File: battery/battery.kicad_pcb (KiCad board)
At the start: 2 copper layers, 73.7 x 63.5 mm, 40 parts, among them J1 batt_1, J2 batt_2, J3 batt_3, J4 batt_4, J5 reed_switch, J6 toPcb+, J7 toPcb-, J8 on_signal, Q1 batt1_sw, Q2 batt2_sw, Q3 batt3_sw, Q4 batt4_sw, Q5 Q_NPN_CBE, U1 LM1117-5.0, U2 LTV-817S

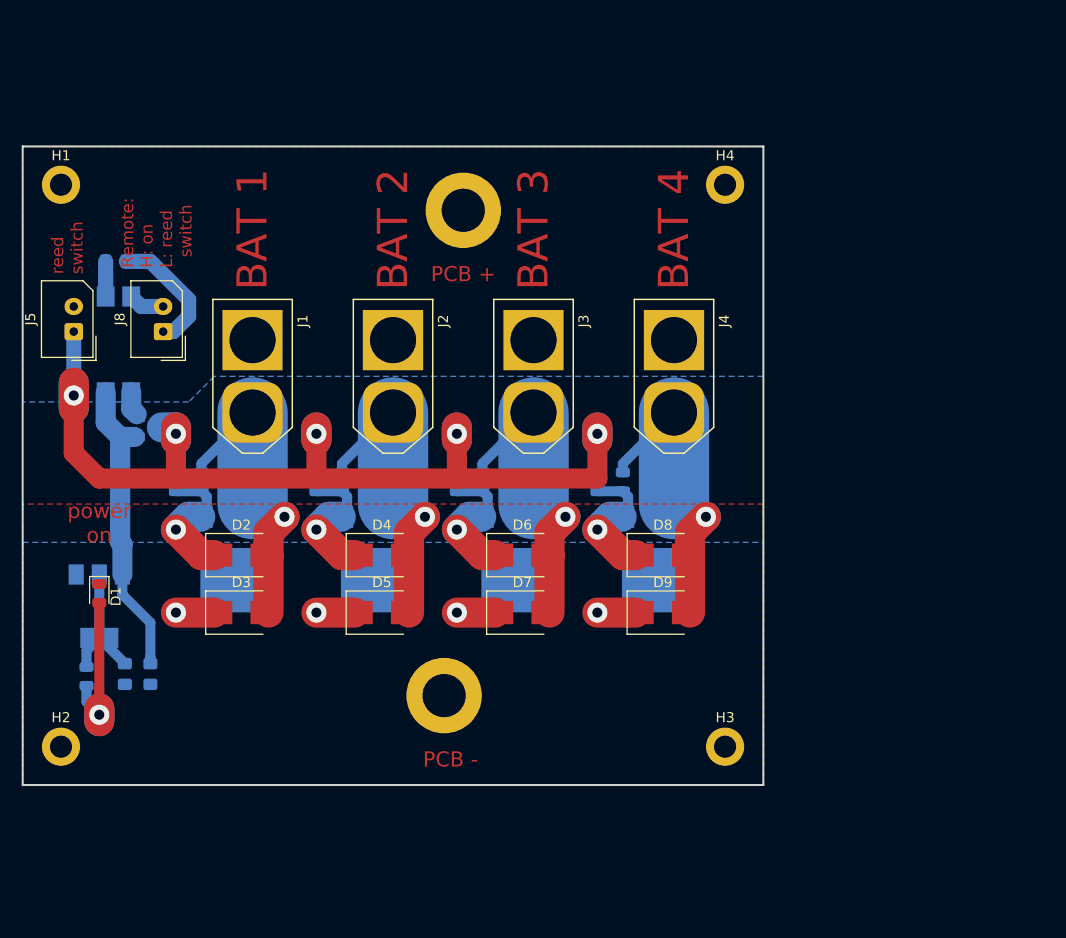
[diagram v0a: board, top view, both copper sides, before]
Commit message: capacitor bybpas
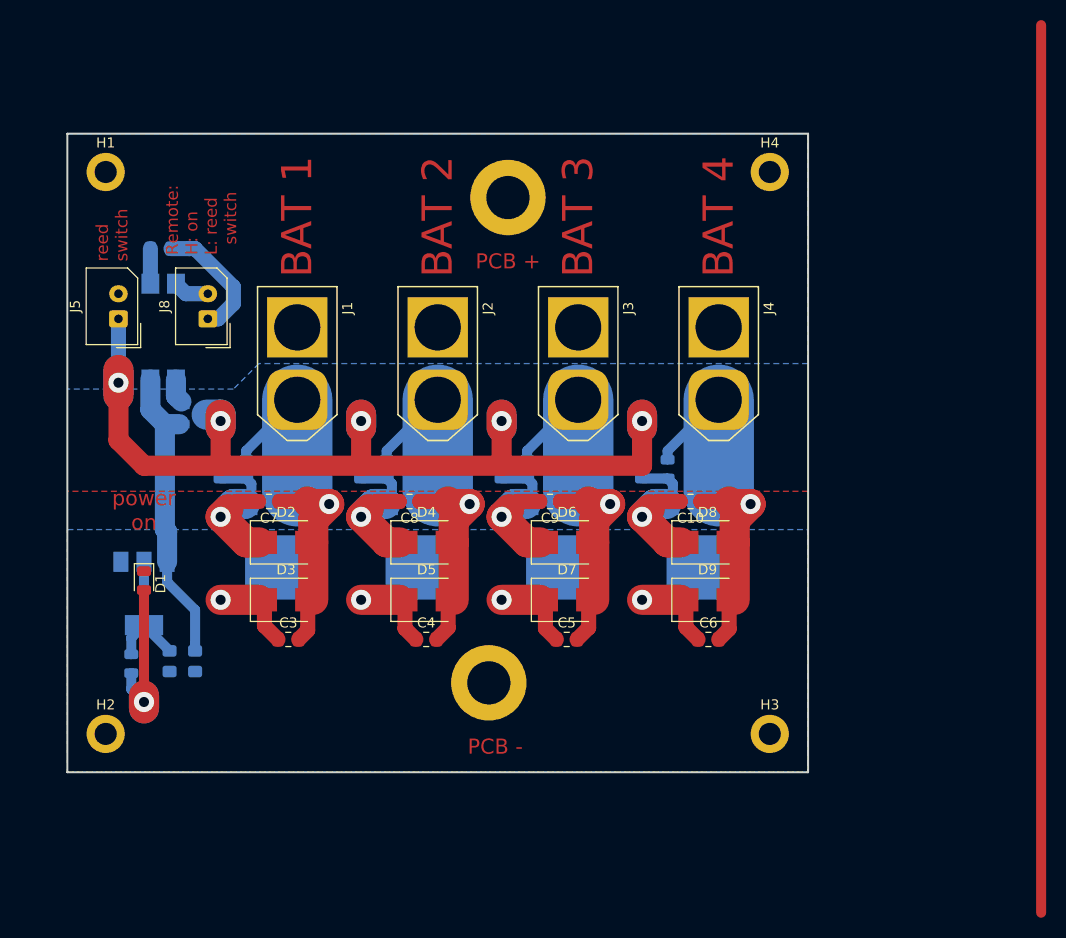
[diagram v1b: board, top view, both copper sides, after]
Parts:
- added C10: 100n, Capacitor_SMD:C_0805_2012Metric_Pad1.15x1.40mm_HandSolder, F.Cu at (117.2, 100.1)
- added C3: 10uF, Capacitor_SMD:C_0805_2012Metric_Pad1.15x1.40mm_HandSolder, F.Cu at (77.2, 113.8)
- added C4: 10uF, Capacitor_SMD:C_0805_2012Metric_Pad1.15x1.40mm_HandSolder, F.Cu at (90.9, 113.8)
- added C5: 10uF, Capacitor_SMD:C_0805_2012Metric_Pad1.15x1.40mm_HandSolder, F.Cu at (104.9, 113.8)
- added C6: 10uF, Capacitor_SMD:C_0805_2012Metric_Pad1.15x1.40mm_HandSolder, F.Cu at (119.0, 113.8)
- added C7: 100n, Capacitor_SMD:C_0805_2012Metric_Pad1.15x1.40mm_HandSolder, F.Cu at (75.3, 100.1)
- added C8: 100n, Capacitor_SMD:C_0805_2012Metric_Pad1.15x1.40mm_HandSolder, F.Cu at (89.3, 100.1)
- added C9: 100n, Capacitor_SMD:C_0805_2012Metric_Pad1.15x1.40mm_HandSolder, F.Cu at (103.2, 100.1)
- C1, C2: value 100n -> C_Small
- moved J6 4.62 mm to (99.1, 69.8)
- moved D2 4.62 mm to (77.0, 104.1)
- moved D3 4.62 mm to (77.0, 109.9)
- moved D4 4.62 mm to (91.0, 104.1)
- moved D5 4.62 mm to (91.0, 109.9)
- moved D6 4.62 mm to (104.9, 104.1)
- moved D7 4.62 mm to (104.9, 109.9)
- moved D8 4.62 mm to (118.9, 104.1)
- moved D9 4.62 mm to (118.9, 109.9)
- moved J1 4.62 mm to (78.1, 86.4)
- moved J2 4.62 mm to (92.1, 86.4)
- moved J3 4.62 mm to (106.0, 86.4)
- moved J4 4.62 mm to (120.0, 86.4)
- moved J7 4.62 mm to (97.2, 118.1)
- moved J8 4.62 mm to (69.2, 81.9)
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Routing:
- net (no net): track 0.00 -> 88.3 mm
- net gnd: track 15.2 -> 33.0 mm
- net Net-(C4-Pad2): track 29.2 -> 43.8 mm
- net Net-(C5-Pad2): track 29.2 -> 43.8 mm
- net Net-(C10-Pad1): track 29.2 -> 43.7 mm
- net Net-(C3-Pad2): track 31.0 -> 40.4 mm
- net Net-(C8-Pad2): track 13.6 -> 21.4 mm
- net Net-(C9-Pad2): track 13.1 -> 20.9 mm
- net Net-(C10-Pad2): track 13.1 -> 20.9 mm
- net Net-(C7-Pad2): track 13.1 -> 18.6 mm

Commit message: fix
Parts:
- removed the C1 at (65.4, 116.0)
- removed the C10 at (117.2, 100.1)
- removed the C2 at (67.9, 116.0)
- removed the C3 at (77.2, 113.8)
- removed the C4 at (90.9, 113.8)
- removed the C5 at (104.9, 113.8)
- removed the C6 at (119.0, 113.8)
- removed the C7 at (75.3, 100.1)
- removed the C8 at (89.3, 100.1)
- removed the C9 at (103.2, 100.1)
- removed the D1 at (62.9, 108.0)
- removed the D2 at (77.0, 104.1)
- removed the D3 at (77.0, 109.9)
- removed the D4 at (91.0, 104.1)
- removed the D5 at (91.0, 109.9)
- removed the D6 at (104.9, 104.1)
- removed the D7 at (104.9, 109.9)
- removed the D8 at (118.9, 104.1)
- removed the D9 at (118.9, 109.9)
- removed the H1 at (59.1, 67.3)
- removed the H2 at (59.1, 123.2)
- removed the H3 at (125.1, 123.2)
- removed the H4 at (125.1, 67.3)
- removed the J1 at (78.1, 86.4)
- removed the J2 at (92.1, 86.4)
- removed the J3 at (106.0, 86.4)
- removed the J4 at (120.0, 86.4)
- removed the J5 at (60.3, 81.9)
- removed the J6 at (99.1, 69.8)
- removed the J7 at (97.2, 118.1)
- removed the J8 at (69.2, 81.9)
- removed the Q1 at (75.8, 104.5)
- removed the Q2 at (89.8, 104.5)
- removed the Q3 at (103.8, 104.5)
- removed the Q4 at (117.7, 104.5)
- removed the Q5 at (67.9, 91.4)
- removed the R1 at (61.6, 116.2)
- removed the R10 at (64.5, 74.9)
- removed the R2 at (70.5, 96.9)
- removed the R3 at (84.5, 96.9)
- removed the R4 at (98.4, 96.9)
- removed the R5 at (112.4, 96.9)
- removed the R6 at (73.0, 96.9)
- removed the R7 at (87.0, 96.9)
- removed the R8 at (101.0, 96.9)
- removed the R9 at (114.9, 96.9)
- removed the U1 at (62.9, 109.2)
- removed the U2 at (64.8, 83.2)
- added C1: C_Small, Capacitor_SMD:C_0805_2012Metric_Pad1.15x1.40mm_HandSolder, B.Cu at (204.7, 68.6)
- added C1: C_Small, Capacitor_SMD:C_0805_2012Metric_Pad1.15x1.40mm_HandSolder, F.Cu at (131.8, 68.6)
- added C10: 100n, Capacitor_SMD:C_0805_2012Metric_Pad1.15x1.40mm_HandSolder, F.Cu at (220.6, 120.4)
- added C10: 100n, Capacitor_SMD:C_0805_2012Metric_Pad1.15x1.40mm_HandSolder, B.Cu at (116.0, 120.4)
- added C2: C_Small, Capacitor_SMD:C_0805_2012Metric_Pad1.15x1.40mm_HandSolder, B.Cu at (204.7, 71.1)
- added C2: C_Small, Capacitor_SMD:C_0805_2012Metric_Pad1.15x1.40mm_HandSolder, F.Cu at (131.8, 71.1)
- added C3: 10uF, Capacitor_SMD:C_0805_2012Metric_Pad1.15x1.40mm_HandSolder, F.Cu at (206.9, 80.4)
- added C3: 10uF, Capacitor_SMD:C_0805_2012Metric_Pad1.15x1.40mm_HandSolder, B.Cu at (129.7, 80.4)
- added C4: 10uF, Capacitor_SMD:C_0805_2012Metric_Pad1.15x1.40mm_HandSolder, F.Cu at (206.9, 94.1)
- added C4: 10uF, Capacitor_SMD:C_0805_2012Metric_Pad1.15x1.40mm_HandSolder, B.Cu at (129.7, 94.1)
- added C5: 10uF, Capacitor_SMD:C_0805_2012Metric_Pad1.15x1.40mm_HandSolder, F.Cu at (206.9, 108.1)
- added C5: 10uF, Capacitor_SMD:C_0805_2012Metric_Pad1.15x1.40mm_HandSolder, B.Cu at (129.7, 108.1)
- added C6: 10uF, Capacitor_SMD:C_0805_2012Metric_Pad1.15x1.40mm_HandSolder, F.Cu at (206.9, 122.2)
- added C6: 10uF, Capacitor_SMD:C_0805_2012Metric_Pad1.15x1.40mm_HandSolder, B.Cu at (129.7, 122.2)
- added C7: 100n, Capacitor_SMD:C_0805_2012Metric_Pad1.15x1.40mm_HandSolder, F.Cu at (220.6, 78.5)
- added C7: 100n, Capacitor_SMD:C_0805_2012Metric_Pad1.15x1.40mm_HandSolder, B.Cu at (116.0, 78.5)
- added C8: 100n, Capacitor_SMD:C_0805_2012Metric_Pad1.15x1.40mm_HandSolder, F.Cu at (220.6, 92.4)
- added C8: 100n, Capacitor_SMD:C_0805_2012Metric_Pad1.15x1.40mm_HandSolder, B.Cu at (116.0, 92.4)
- added C9: 100n, Capacitor_SMD:C_0805_2012Metric_Pad1.15x1.40mm_HandSolder, F.Cu at (220.6, 106.4)
- added C9: 100n, Capacitor_SMD:C_0805_2012Metric_Pad1.15x1.40mm_HandSolder, B.Cu at (116.0, 106.4)
- added D1: power_ok, LED_SMD:LED_0805_2012Metric, F.Cu at (212.7, 66.0)
- added D1: power_ok, LED_SMD:LED_0805_2012Metric, B.Cu at (123.8, 66.0)
- added D2: D_TVS, Diode_SMD:D_SMB, F.Cu at (216.5, 80.2)
- added D2: D_TVS, Diode_SMD:D_SMB, B.Cu at (120.0, 80.2)
- added D3: D_TVS, Diode_SMD:D_SMB, F.Cu at (210.8, 80.2)
- added D3: D_TVS, Diode_SMD:D_SMB, B.Cu at (125.7, 80.2)
- added D4: D_TVS, Diode_SMD:D_SMB, F.Cu at (216.5, 94.1)
- added D4: D_TVS, Diode_SMD:D_SMB, B.Cu at (120.0, 94.1)
- added D5: D_TVS, Diode_SMD:D_SMB, F.Cu at (210.8, 94.1)
- added D5: D_TVS, Diode_SMD:D_SMB, B.Cu at (125.7, 94.1)
- added D6: D_TVS, Diode_SMD:D_SMB, F.Cu at (216.5, 108.1)
- added D6: D_TVS, Diode_SMD:D_SMB, B.Cu at (120.0, 108.1)
- added D7: D_TVS, Diode_SMD:D_SMB, F.Cu at (210.8, 108.1)
- added D7: D_TVS, Diode_SMD:D_SMB, B.Cu at (125.7, 108.1)
- added D8: D_TVS, Diode_SMD:D_SMB, F.Cu at (216.5, 122.1)
- added D8: D_TVS, Diode_SMD:D_SMB, B.Cu at (120.0, 122.1)
- added D9: D_TVS, Diode_SMD:D_SMB, F.Cu at (210.8, 122.1)
- added D9: D_TVS, Diode_SMD:D_SMB, B.Cu at (125.7, 122.1)
- added H1: mnt, MountingHole:MountingHole_2.2mm_M2_DIN965_Pad, F.Cu at (253.4, 62.2)
- added H1: mnt, MountingHole:MountingHole_2.2mm_M2_DIN965_Pad, B.Cu at (83.2, 62.2)
- added H2: mnt, MountingHole:MountingHole_2.2mm_M2_DIN965_Pad, F.Cu at (197.5, 62.2)
- added H2: mnt, MountingHole:MountingHole_2.2mm_M2_DIN965_Pad, B.Cu at (139.1, 62.2)
- added H3: mnt, MountingHole:MountingHole_2.2mm_M2_DIN965_Pad, F.Cu at (197.5, 128.3)
- added H3: mnt, MountingHole:MountingHole_2.2mm_M2_DIN965_Pad, B.Cu at (139.1, 128.3)
- added H4: mnt, MountingHole:MountingHole_2.2mm_M2_DIN965_Pad, F.Cu at (253.4, 128.3)
- added H4: mnt, MountingHole:MountingHole_2.2mm_M2_DIN965_Pad, B.Cu at (83.2, 128.3)
- added J1: batt_1, power_connectors:XT60UPB-M, F.Cu at (234.3, 81.3)
- added J1: batt_1, power_connectors:XT60UPB-M, B.Cu at (102.2, 81.3)
- added J2: batt_2, power_connectors:XT60UPB-M, F.Cu at (234.3, 95.2)
- added J2: batt_2, power_connectors:XT60UPB-M, B.Cu at (102.2, 95.2)
- added J3: batt_3, power_connectors:XT60UPB-M, F.Cu at (234.3, 109.2)
- added J3: batt_3, power_connectors:XT60UPB-M, B.Cu at (102.2, 109.2)
- added J4: batt_4, power_connectors:XT60UPB-M, F.Cu at (234.3, 123.2)
- added J4: batt_4, power_connectors:XT60UPB-M, B.Cu at (102.2, 123.2)
- added J5: reed_switch, Connector_Molex:Molex_SPOX_5267-02A_1x02_P2.50mm_Vertical, F.Cu at (238.8, 63.5)
- added J5: reed_switch, Connector_Molex:Molex_SPOX_5267-02A_1x02_P2.50mm_Vertical, B.Cu at (97.8, 63.5)
- added J6: toPcb+, MountingHole:MountingHole_4.3mm_M4_DIN965_Pad, B.Cu at (250.8, 102.2)
- added J6: toPcb+, MountingHole:MountingHole_4.3mm_M4_DIN965_Pad, F.Cu at (85.7, 102.2)
- added J7: toPcb-, MountingHole:MountingHole_4.3mm_M4_DIN965_Pad, B.Cu at (202.6, 100.3)
- added J7: toPcb-, MountingHole:MountingHole_4.3mm_M4_DIN965_Pad, F.Cu at (134.0, 100.3)
- added J8: on_signal, Connector_Molex:Molex_SPOX_5267-02A_1x02_P2.50mm_Vertical, F.Cu at (238.8, 72.4)
- added J8: on_signal, Connector_Molex:Molex_SPOX_5267-02A_1x02_P2.50mm_Vertical, B.Cu at (97.8, 72.4)
- added Q1: batt1_sw, Package_TO_SOT_SMD:TO-252-2, B.Cu at (216.1, 79.0)
- added Q1: batt1_sw, Package_TO_SOT_SMD:TO-252-2, F.Cu at (120.4, 79.0)
- added Q2: batt2_sw, Package_TO_SOT_SMD:TO-252-2, B.Cu at (216.1, 93.0)
- added Q2: batt2_sw, Package_TO_SOT_SMD:TO-252-2, F.Cu at (120.4, 93.0)
- added Q3: batt3_sw, Package_TO_SOT_SMD:TO-252-2, B.Cu at (216.1, 106.9)
- added Q3: batt3_sw, Package_TO_SOT_SMD:TO-252-2, F.Cu at (120.4, 106.9)
- added Q4: batt4_sw, Package_TO_SOT_SMD:TO-252-2, B.Cu at (216.1, 120.9)
- added Q4: batt4_sw, Package_TO_SOT_SMD:TO-252-2, F.Cu at (120.4, 120.9)
- added Q5: Q_NPN_CBE, Package_TO_SOT_SMD:SOT-23, B.Cu at (229.2, 71.1)
- added Q5: Q_NPN_CBE, Package_TO_SOT_SMD:SOT-23, F.Cu at (107.3, 71.1)
- added R1: 400, Resistor_SMD:R_0805_2012Metric, B.Cu at (204.5, 64.8)
- added R1: 400, Resistor_SMD:R_0805_2012Metric, F.Cu at (132.1, 64.8)
- added R10: R, Resistor_SMD:R_0805_2012Metric_Pad1.15x1.40mm_HandSolder, B.Cu at (245.7, 67.7)
- added R10: R, Resistor_SMD:R_0805_2012Metric_Pad1.15x1.40mm_HandSolder, F.Cu at (90.8, 67.7)
- added R2: 100, Resistor_SMD:R_0805_2012Metric, B.Cu at (223.8, 73.7)
- added R2: 100, Resistor_SMD:R_0805_2012Metric, F.Cu at (112.7, 73.7)
- added R3: 100, Resistor_SMD:R_0805_2012Metric, B.Cu at (223.8, 87.6)
- added R3: 100, Resistor_SMD:R_0805_2012Metric, F.Cu at (112.7, 87.6)
- added R4: 100, Resistor_SMD:R_0805_2012Metric, B.Cu at (223.8, 101.6)
- added R4: 100, Resistor_SMD:R_0805_2012Metric, F.Cu at (112.7, 101.6)
- added R5: 100, Resistor_SMD:R_0805_2012Metric, B.Cu at (223.8, 115.6)
- added R5: 100, Resistor_SMD:R_0805_2012Metric, F.Cu at (112.7, 115.6)
- added R6: 47k, Resistor_SMD:R_0805_2012Metric, B.Cu at (223.8, 76.2)
- added R6: 47k, Resistor_SMD:R_0805_2012Metric, F.Cu at (112.7, 76.2)
- added R7: 47k, Resistor_SMD:R_0805_2012Metric, B.Cu at (223.8, 90.2)
- added R7: 47k, Resistor_SMD:R_0805_2012Metric, F.Cu at (112.7, 90.2)
- added R8: 47k, Resistor_SMD:R_0805_2012Metric, B.Cu at (223.8, 104.1)
- added R8: 47k, Resistor_SMD:R_0805_2012Metric, F.Cu at (112.7, 104.1)
- added R9: 47k, Resistor_SMD:R_0805_2012Metric, B.Cu at (223.8, 118.1)
- added R9: 47k, Resistor_SMD:R_0805_2012Metric, F.Cu at (112.7, 118.1)
- added U1: LM1117-5.0, Package_TO_SOT_SMD:SOT-223-3_TabPin2, B.Cu at (211.5, 66.0)
- added U1: LM1117-5.0, Package_TO_SOT_SMD:SOT-223-3_TabPin2, F.Cu at (125.1, 66.0)
- added U2: LTV-817S, Package_DIP:SMDIP-4_W9.53mm, B.Cu at (237.5, 67.9)
- added U2: LTV-817S, Package_DIP:SMDIP-4_W9.53mm, F.Cu at (99.1, 67.9)
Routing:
- net Net-(J5-Pad1): track 115.6 -> 231.2 mm, vias 5 -> 10
- net Net-(C5-Pad2): track 43.8 -> 87.6 mm, vias 1 -> 2
- net Net-(C4-Pad2): track 43.8 -> 87.6 mm, vias 1 -> 2
- net Net-(C10-Pad1): track 43.7 -> 87.5 mm, vias 1 -> 2
- net Net-(C3-Pad2): track 40.4 -> 80.8 mm, vias 1 -> 2
- net gnd: track 33.0 -> 65.9 mm, vias 4 -> 8
- net Vin: track 30.3 -> 60.6 mm
- net Net-(C8-Pad2): track 21.4 -> 42.7 mm, vias 1 -> 2
- net Net-(C9-Pad2): track 20.9 -> 41.7 mm, vias 1 -> 2
- net Net-(C10-Pad2): track 20.9 -> 41.7 mm, vias 1 -> 2
- net Net-(C7-Pad2): track 18.6 -> 37.2 mm, vias 1 -> 2
- net Net-(D1-Pad2): track 17.1 -> 34.1 mm, vias 1 -> 2
- net Net-(C1-Pad1): track 13.3 -> 26.7 mm
- net Net-(J8-Pad1): track 12.6 -> 25.2 mm
- net Net-(J8-Pad2): track 3.59 -> 7.17 mm
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- added copper zone on F.Cu, net Vin
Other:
- board size 73.7 x 63.5 mm -> 177.8 x 73.7 mm

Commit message: new schematic
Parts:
- removed the C1 at (204.7, 68.6)
- removed the C10 at (220.6, 120.4)
- removed the C10 at (116.0, 120.4)
- removed the C2 at (204.7, 71.1)
- removed the C3 at (206.9, 80.4)
- removed the C3 at (129.7, 80.4)
- removed the C4 at (206.9, 94.1)
- removed the C4 at (129.7, 94.1)
- removed the C5 at (206.9, 108.1)
- removed the C5 at (129.7, 108.1)
- removed the C6 at (206.9, 122.2)
- removed the C6 at (129.7, 122.2)
- removed the C7 at (220.6, 78.5)
- removed the C8 at (220.6, 92.4)
- removed the C8 at (116.0, 92.4)
- removed the C9 at (220.6, 106.4)
- removed the C9 at (116.0, 106.4)
- removed the D1 at (212.7, 66.0)
- removed the D2 at (216.5, 80.2)
- removed the D3 at (210.8, 80.2)
- removed the D4 at (216.5, 94.1)
- removed the D4 at (120.0, 94.1)
- removed the D5 at (210.8, 94.1)
- removed the D5 at (125.7, 94.1)
- removed the D6 at (216.5, 108.1)
- removed the D6 at (120.0, 108.1)
- removed the D7 at (210.8, 108.1)
- removed the D7 at (125.7, 108.1)
- removed the D8 at (216.5, 122.1)
- removed the D8 at (120.0, 122.1)
- removed the D9 at (210.8, 122.1)
- removed the D9 at (125.7, 122.1)
- removed the H1 at (253.4, 62.2)
- removed the H2 at (197.5, 62.2)
- removed the H3 at (197.5, 128.3)
- removed the H3 at (139.1, 128.3)
- removed the H4 at (253.4, 128.3)
- removed the J1 at (234.3, 81.3)
- removed the J2 at (234.3, 95.2)
- removed the J2 at (102.2, 95.2)
- removed the J3 at (234.3, 109.2)
- removed the J3 at (102.2, 109.2)
- removed the J4 at (234.3, 123.2)
- removed the J4 at (102.2, 123.2)
- removed the J5 at (238.8, 63.5)
- removed the J6 at (250.8, 102.2)
- removed the J7 at (202.6, 100.3)
- removed the J8 at (238.8, 72.4)
- removed the Q1 at (216.1, 79.0)
- removed the Q1 at (120.4, 79.0)
- removed the Q2 at (216.1, 93.0)
- removed the Q2 at (120.4, 93.0)
- removed the Q3 at (216.1, 106.9)
- removed the Q3 at (120.4, 106.9)
- removed the Q4 at (216.1, 120.9)
- removed the Q4 at (120.4, 120.9)
- removed the Q5 at (229.2, 71.1)
- removed the Q5 at (107.3, 71.1)
- removed the R1 at (204.5, 64.8)
- removed the R10 at (245.7, 67.7)
- removed the R2 at (223.8, 73.7)
- removed the R3 at (223.8, 87.6)
- removed the R4 at (223.8, 101.6)
- removed the R4 at (112.7, 101.6)
- removed the R5 at (223.8, 115.6)
- removed the R5 at (112.7, 115.6)
- removed the R6 at (223.8, 76.2)
- removed the R7 at (223.8, 90.2)
- removed the R7 at (112.7, 90.2)
- removed the R8 at (223.8, 104.1)
- removed the R8 at (112.7, 104.1)
- removed the R9 at (223.8, 118.1)
- removed the R9 at (112.7, 118.1)
- removed the U1 at (211.5, 66.0)
- removed the U2 at (237.5, 67.9)
- added C10: 100n, Capacitor_SMD:C_0805_2012Metric_Pad1.15x1.40mm_HandSolder, B.Cu at (164.8, 87.2)
- added C3: 10uF, Capacitor_SMD:C_1206_3216Metric_Pad1.42x1.75mm_HandSolder, B.Cu at (121.0, 73.5)
- added C4: 10uF, Capacitor_SMD:C_1206_3216Metric_Pad1.42x1.75mm_HandSolder, B.Cu at (136.0, 73.5)
- added C5: 10uF, Capacitor_SMD:C_1206_3216Metric_Pad1.42x1.75mm_HandSolder, B.Cu at (151.3, 73.5)
- added C6: 10uF, Capacitor_SMD:C_1206_3216Metric_Pad1.42x1.75mm_HandSolder, B.Cu at (166.6, 73.5)
- added C8: 100n, Capacitor_SMD:C_0805_2012Metric_Pad1.15x1.40mm_HandSolder, B.Cu at (134.4, 87.2)
- added C9: 100n, Capacitor_SMD:C_0805_2012Metric_Pad1.15x1.40mm_HandSolder, B.Cu at (149.6, 87.2)
- added D10: bat48, Diode_THT:D_DO-35_SOD27_P10.16mm_Horizontal, B.Cu at (113.0, 90.2)
- added D11: bat48, Diode_THT:D_DO-35_SOD27_P10.16mm_Horizontal, B.Cu at (128.3, 90.2)
- added D12: bat48, Diode_THT:D_DO-35_SOD27_P10.16mm_Horizontal, B.Cu at (143.5, 90.2)
- added D13: bat48, Diode_THT:D_DO-35_SOD27_P10.16mm_Horizontal, B.Cu at (158.8, 90.2)
- added D4: D_TVS, Diode_SMD:D_SMB, B.Cu at (136.1, 83.2)
- added D5: D_TVS, Diode_SMD:D_SMB, B.Cu at (136.1, 77.5)
- added D6: D_TVS, Diode_SMD:D_SMB, B.Cu at (151.3, 83.2)
- added D7: D_TVS, Diode_SMD:D_SMB, B.Cu at (151.3, 77.5)
- added D8: D_TVS, Diode_SMD:D_SMB, B.Cu at (166.5, 83.2)
- added D9: D_TVS, Diode_SMD:D_SMB, B.Cu at (166.5, 77.5)
- added H3: mnt, MountingHole:MountingHole_2.2mm_M2_DIN965_Pad, B.Cu at (184.2, 64.1)
- added J2: batt_2, power_connectors:XT60UPB-M, B.Cu at (137.2, 101.0)
- added J3: batt_3, power_connectors:XT60UPB-M, B.Cu at (152.4, 101.0)
- added J4: batt_4, power_connectors:XT60UPB-M, B.Cu at (167.6, 101.0)
- added Q1: batt1_sw, Package_TO_SOT_SMD:TO-263-2, F.Cu at (119.6, 80.0)
- added Q2: batt2_sw, Package_TO_SOT_SMD:TO-263-2, F.Cu at (134.9, 80.3)
- added Q3: batt3_sw, Package_TO_SOT_SMD:TO-263-2, F.Cu at (150.1, 80.3)
- added Q4: batt4_sw, Package_TO_SOT_SMD:TO-263-2, F.Cu at (165.4, 80.3)
- added Q5: BC817-25, Package_TO_SOT_SMD:SOT-23_Handsoldering, F.Cu at (108.0, 95.9)
- added R11: 10k, Resistor_SMD:R_0805_2012Metric, F.Cu at (113.6, 99.3)
- added R4: 100, Resistor_SMD:R_0805_2012Metric, F.Cu at (144.1, 95.6)
- added R5: 100, Resistor_SMD:R_0805_2012Metric, F.Cu at (159.4, 95.6)
- added R7: 47k, Resistor_SMD:R_0805_2012Metric, F.Cu at (131.4, 97.5)
- added R8: 47k, Resistor_SMD:R_0805_2012Metric, F.Cu at (146.7, 97.5)
- added R9: 47k, Resistor_SMD:R_0805_2012Metric, F.Cu at (161.9, 97.5)
- R10: value R -> 680
- moved H4 101.3 mm to (184.2, 120.0), turned to 0 degrees
- moved J6 94.2 mm to (179.7, 109.2), turned to 0 degrees
- moved H1 61.0 mm to (102.9, 120.0), turned to 0 degrees
- moved R10 48.0 mm to (108.3, 112.4), turned to 0 degrees
- moved J7 46.2 mm to (179.7, 94.0), turned to 0 degrees
- moved J5 42.4 mm to (104.1, 105.4), turned to 270 degrees
- moved U2 37.4 mm to (108.6, 104.1), turned to 90 degrees
- moved J8 36.4 mm to (113.0, 105.4), turned to 270 degrees
- moved H2 36.2 mm to (102.9, 64.1), turned to 0 degrees
- moved J1 27.8 mm to (121.9, 101.0), turned to 90 degrees
- moved R1 27.4 mm to (105.4, 71.1), turned to 270 degrees
- moved C1 22.8 mm to (109.2, 71.4), turned to 90 degrees
- moved U1 22.0 mm to (106.7, 78.1), turned to 90 degrees
- moved R2 21.9 mm to (113.7, 95.6), turned to 90 degrees
- moved D1 21.7 mm to (106.7, 79.4), turned to 90 degrees
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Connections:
- J5 pad 1: Net-(J5-Pad1) -> Net-(D10-Pad2)
- R2 pad 2: Net-(J5-Pad1) -> Net-(D10-Pad1)
- R3 pad 2: Net-(J5-Pad1) -> Net-(D11-Pad1)
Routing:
- net (no net): track 88.3 -> 396.2 mm
- net Net-(J5-Pad1): track 231.2 -> 0.00 mm, vias 10 -> 0
- net Net-(D10-Pad2): track 0.00 -> 86.3 mm, vias 0 -> 2
- net Net-(C5-Pad2): track 87.6 -> 41.7 mm, vias 2 -> 1
- net Net-(C4-Pad2): track 87.6 -> 41.7 mm, vias 2 -> 1
- net Net-(C10-Pad1): track 87.5 -> 41.6 mm, vias 2 -> 1
- net Net-(C3-Pad2): track 80.8 -> 40.7 mm, vias 2 -> 1
- net Vin: track 60.6 -> 92.3 mm
- net gnd: track 65.9 -> 87.1 mm, vias 8 -> 3
- net Net-(D1-Pad2): track 34.1 -> 17.1 mm, vias 2 -> 1
- net Net-(C8-Pad2): track 42.7 -> 28.1 mm, vias 2 -> 1
- net Net-(C10-Pad2): track 41.7 -> 27.6 mm, vias 2 -> 1
- net Net-(C1-Pad1): track 26.7 -> 13.3 mm
- net Net-(C9-Pad2): track 41.7 -> 28.4 mm, vias 2 -> 1
- net Net-(J8-Pad1): track 25.2 -> 12.6 mm
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- removed copper zone on B.Cu, net Vin
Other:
- board size 177.8 x 73.7 mm -> 88.9 x 63.5 mm

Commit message: power traces
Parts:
- moved J6 1.27 mm to (179.7, 108.0)
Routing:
- net Vin: track 92.3 -> 92.8 mm, vias 0 -> 4
- net gnd: vias 3 -> 8
